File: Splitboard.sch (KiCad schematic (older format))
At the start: 5 parts

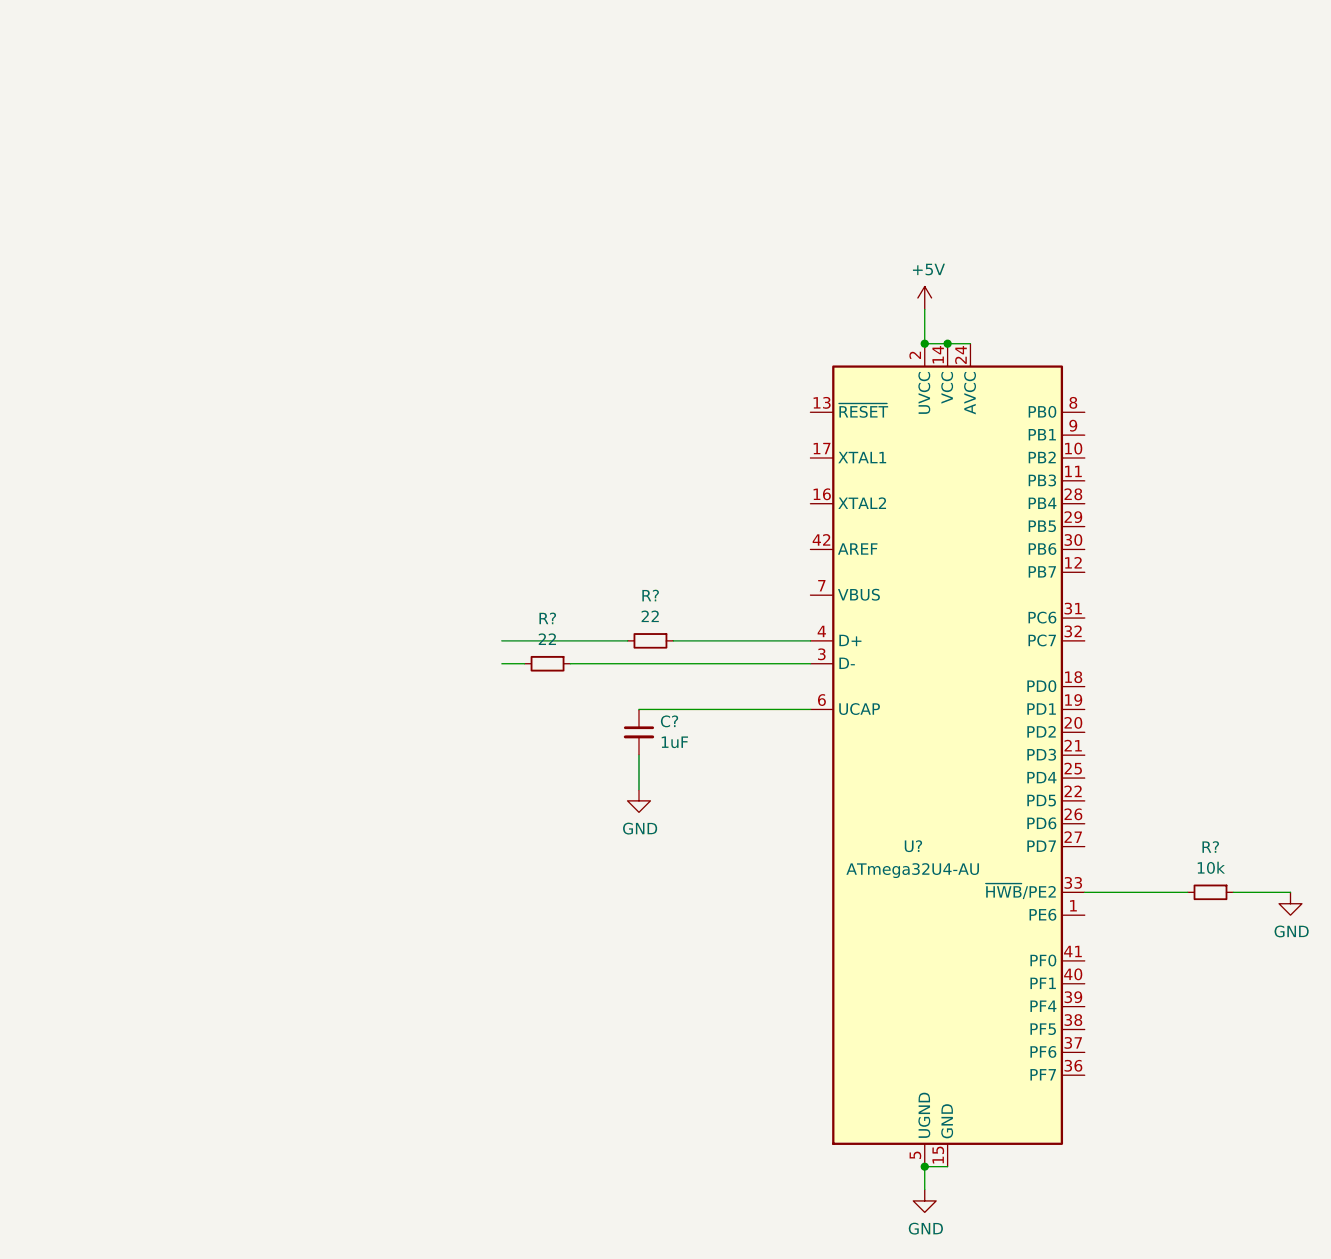
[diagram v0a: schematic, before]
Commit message: Add submodules
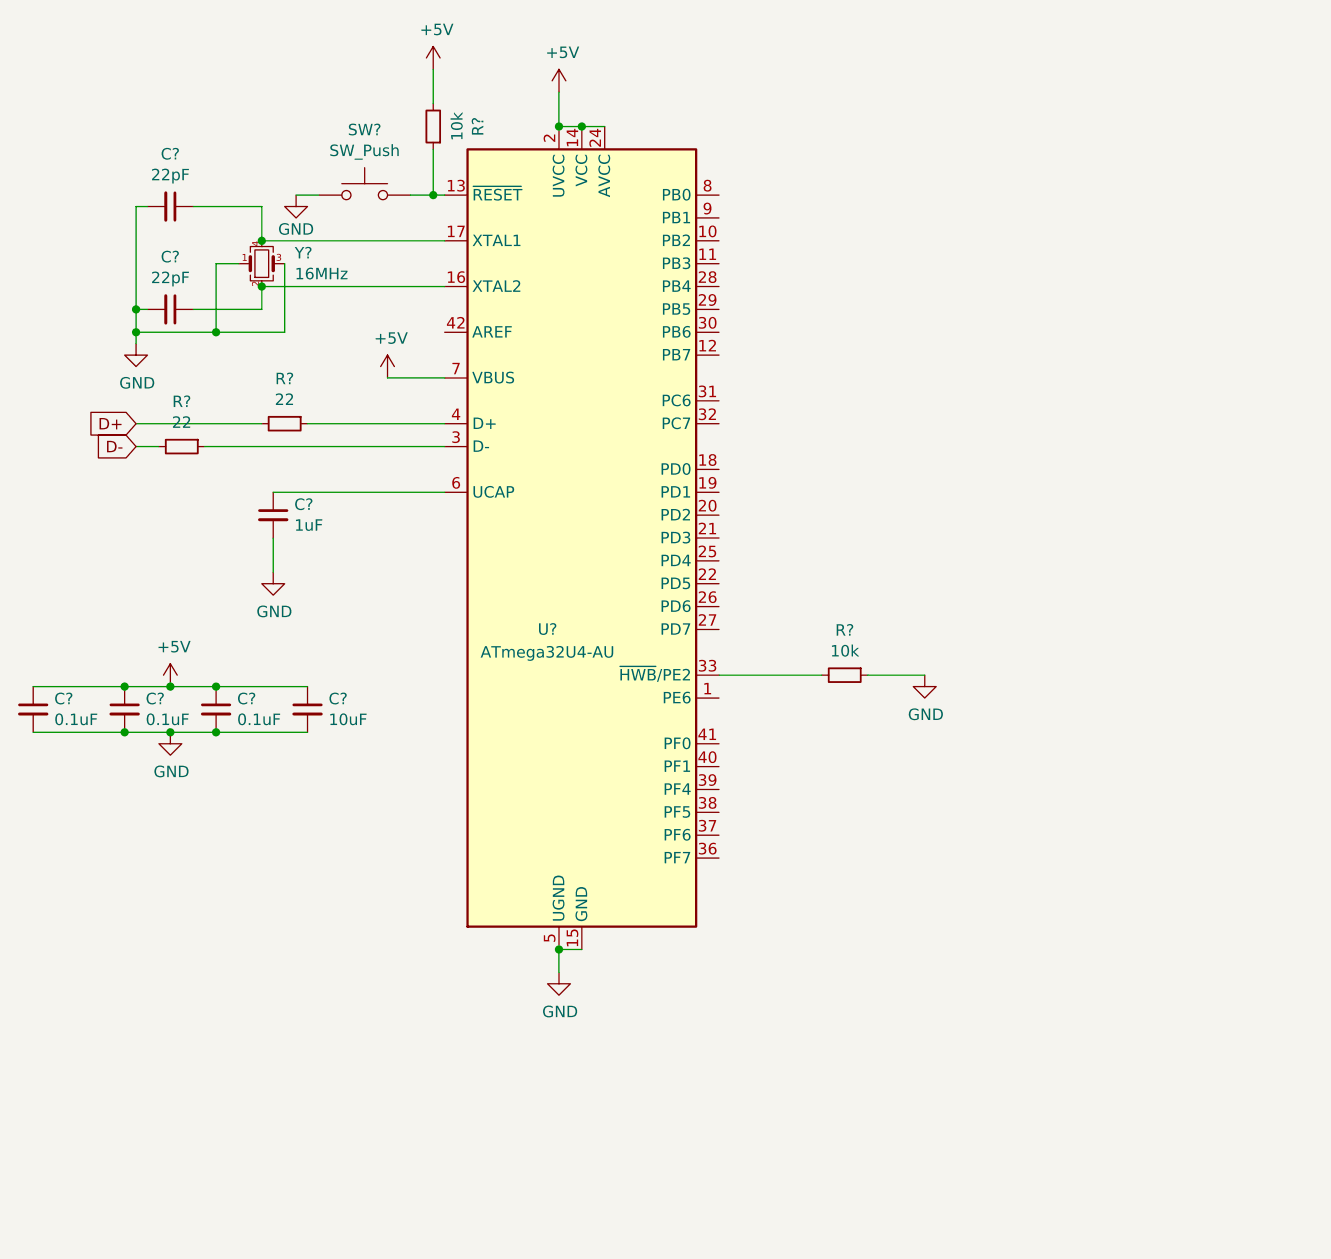
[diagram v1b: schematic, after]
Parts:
- added C? (x3): 0.1uF, symbol Device:C_Small
- added C?: 10uF, symbol Device:C_Small
- added C? (x2): 22pF, symbol Device:C_Small
- added R?: 10k, symbol Device:R_Small
- added SW?: SW_Push, symbol Switch:SW_Push
- added Y?: 16MHz, symbol Device:Crystal_GND24_Small
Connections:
- net labels added: D+, D-
- wire segments 13 -> 43
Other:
- moved on the sheet: C?, R?, U?

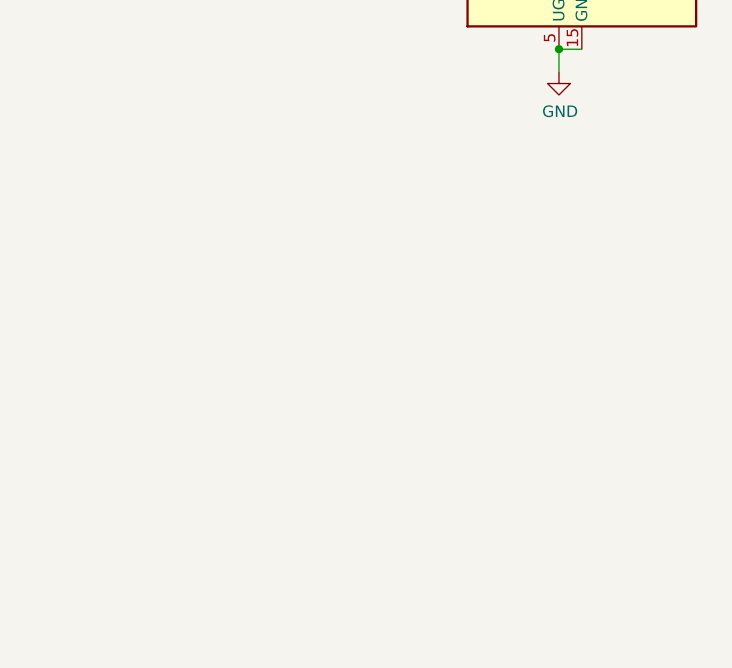
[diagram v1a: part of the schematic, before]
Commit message: basic layout no switches
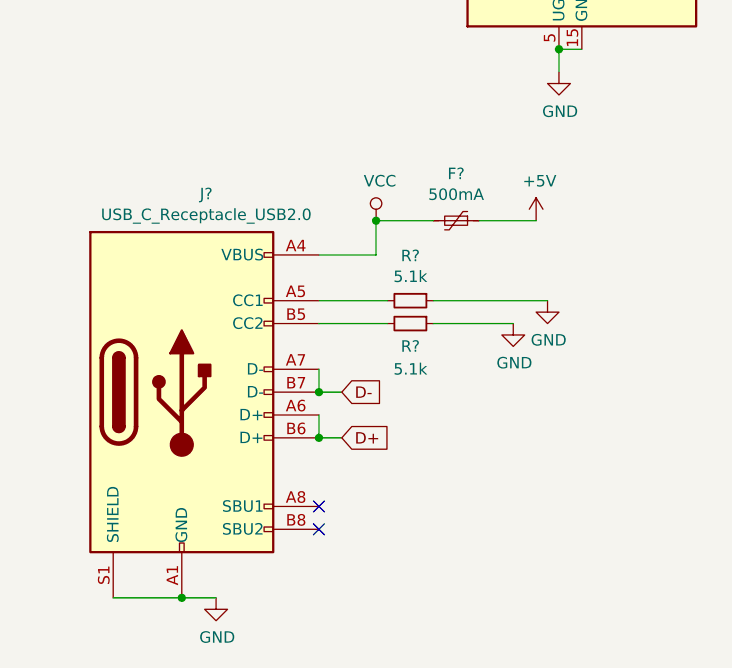
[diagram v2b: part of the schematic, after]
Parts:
- added F?: 500mA, symbol Device:Polyfuse_Small
- added J?: USB_C_Receptacle_USB2.0, symbol Connector:USB_C_Receptacle_USB2.0
- added R? (x2): 5.1k, symbol Device:R_Small
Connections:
- net +5V: now also F?.1
- net D+: now also J?.A6 (D+), J?.B6 (D+)
- net D-: now also J?.A7 (D-), J?.B7 (D-)
- net GND: now also J?.A1 (GND), J?.A12 (GND), J?.B1 (GND), J?.B12 (GND), J?.S1 (SHIELD), R?.1, R?.1
- new net: J?.A5 (CC1), R?.2
- new net: J?.B5 (CC2), R?.2
- new net VCC: F?.2, J?.A4 (VBUS), J?.A9 (VBUS), J?.B4 (VBUS), J?.B9 (VBUS)
- no-connect marks 0 -> 2
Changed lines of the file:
@@
 Text GLabel 1200 2400 0    50   Input ~ 0
 D-
+$Comp
+L Connector:USB_C_Receptacle_USB2.0 J?
+U 1 1 5F4D72AE
+P 1400 6100
+F 0 "J?" H 1507 6967 50  0000 C CNN
+F 1 "USB_C_Receptacle_USB2.0" H 1507 6876 50  0000 C CNN
+F 2 "" H 1550 6100 50  0001 C CNN
+F 3 "https://www.usb.org/sites/default/files/documents/usb_type-c.zip" H 1550 6100 50  0001 C CNN
+	1    1400 6100
+	1    0    0    -1
+$EndComp
+$Comp
+L Device:R_Small R?
+U 1 1 5F4DA8E6
+P 2400 5700
+F 0 "R?" V 2204 5700 50  0000 C CNN
+F 1 "5.1k" V 2295 5700 50  0000 C CNN
+F 2 "" H 2400 5700 50  0001 C CNN
+F 3 "~" H 2400 5700 50  0001 C CNN
+	1    2400 5700
+	0    1    1    0
+$EndComp
+$Comp
+L Device:R_Small R?
+U 1 1 5F4DB46A
+P 2400 5800
+F 0 "R?" V 2500 5800 50  0000 C CNN
+F 1 "5.1k" V 2600 5800 50  0000 C CNN
+F 2 "" H 2400 5800 50  0001 C CNN
+F 3 "~" H 2400 5800 50  0001 C CNN
+	1    2400 5800
+	0    1    1    0
+$EndComp
+$Comp
+L power:GND #PWR?
+U 1 1 5F4DBB17
+P 2850 5800
+F 0 "#PWR?" H 2850 5550 50  0001 C CNN
+F 1 "GND" H 2855 5627 50  0000 C CNN
+F 2 "" H 2850 5800 50  0001 C CNN
+F 3 "" H 2850 5800 50  0001 C CNN
+	1    2850 5800
+	1    0    0    -1
+$EndComp
+$Comp
+L power:GND #PWR?
+U 1 1 5F4DC6DD
+P 3000 5700
+F 0 "#PWR?" H 3000 5450 50  0001 C CNN
+F 1 "GND" H 3005 5527 50  0000 C CNN
+F 2 "" H 3000 5700 50  0001 C CNN
+F 3 "" H 3000 5700 50  0001 C CNN
+	1    3000 5700
+	1    0    0    -1
+$EndComp
+Wire Wire Line
+	3000 5700 2500 5700
+Wire Wire Line
+	2850 5800 2500 5800
+Wire Wire Line
+	2300 5800 2000 5800
+Wire Wire Line
+	2300 5700 2000 5700
+Wire Wire Line
+	2000 6000 2000 6100
+Wire Wire Line
+	2000 6100 2100 6100
+Connection ~ 2000 6100
+Wire Wire Line
+	2000 6200 2000 6300
+Wire Wire Line
+	2000 6300 2100 6300
+Connection ~ 2000 6300
+NoConn ~ 2000 6600
+NoConn ~ 2000 6700
+$Comp
+L power:VCC #PWR?
+U 1 1 5F4E5B6C
+P 2250 5350
+F 0 "#PWR?" H 2250 5200 50  0001 C CNN
+F 1 "VCC" H 2267 5523 50  0000 C CNN
+F 2 "" H 2250 5350 50  0001 C CNN
+F 3 "" H 2250 5350 50  0001 C CNN
+	1    2250 5350
+	1    0    0    -1
+$EndComp
+Wire Wire Line
+	2000 5500 2250 5500
+Wire Wire Line
+	2250 5500 2250 5350
+$Comp
+L Device:Polyfuse_Small F?
+U 1 1 5F4E76E9
+P 2600 5350
+F 0 "F?" V 2395 5350 50  0000 C CNN
+F 1 "500mA" V 2486 5350 50  0000 C CNN
+F 2 "" H 2650 5150 50  0001 L CNN
+F 3 "~" H 2600 5350 50  0001 C CNN
+	1    2600 5350
+	0    1    1    0
+$EndComp
+Wire Wire Line
+	2250 5350 2500 5350
+Connection ~ 2250 5350
+$Comp
+L power:+5V #PWR?
+U 1 1 5F4E9BB4
+P 2950 5350
+F 0 "#PWR?" H 2950 5200 50  0001 C CNN
+F 1 "+5V" H 2965 5523 50  0000 C CNN
+F 2 "" H 2950 5350 50  0001 C CNN
+F 3 "" H 2950 5350 50  0001 C CNN
+	1    2950 5350
+	1    0    0    -1
+$EndComp
+Wire Wire Line
+	2700 5350 2950 5350
+Text GLabel 2100 6300 2    50   Input ~ 0
+D+
+Text GLabel 2100 6100 2    50   Input ~ 0
+D-
+Wire Wire Line
+	1100 7000 1400 7000
+Connection ~ 1400 7000
+Wire Wire Line
+	1400 7000 1550 7000
+$Comp
+L power:GND #PWR?
+U 1 1 5F4EEDED
+P 1550 7000
+F 0 "#PWR?" H 1550 6750 50  0001 C CNN
+F 1 "GND" H 1555 6827 50  0000 C CNN
+F 2 "" H 1550 7000 50  0001 C CNN
+F 3 "" H 1550 7000 50  0001 C CNN
+	1    1550 7000
+	1    0    0    -1
+$EndComp
 $EndSCHEMATC

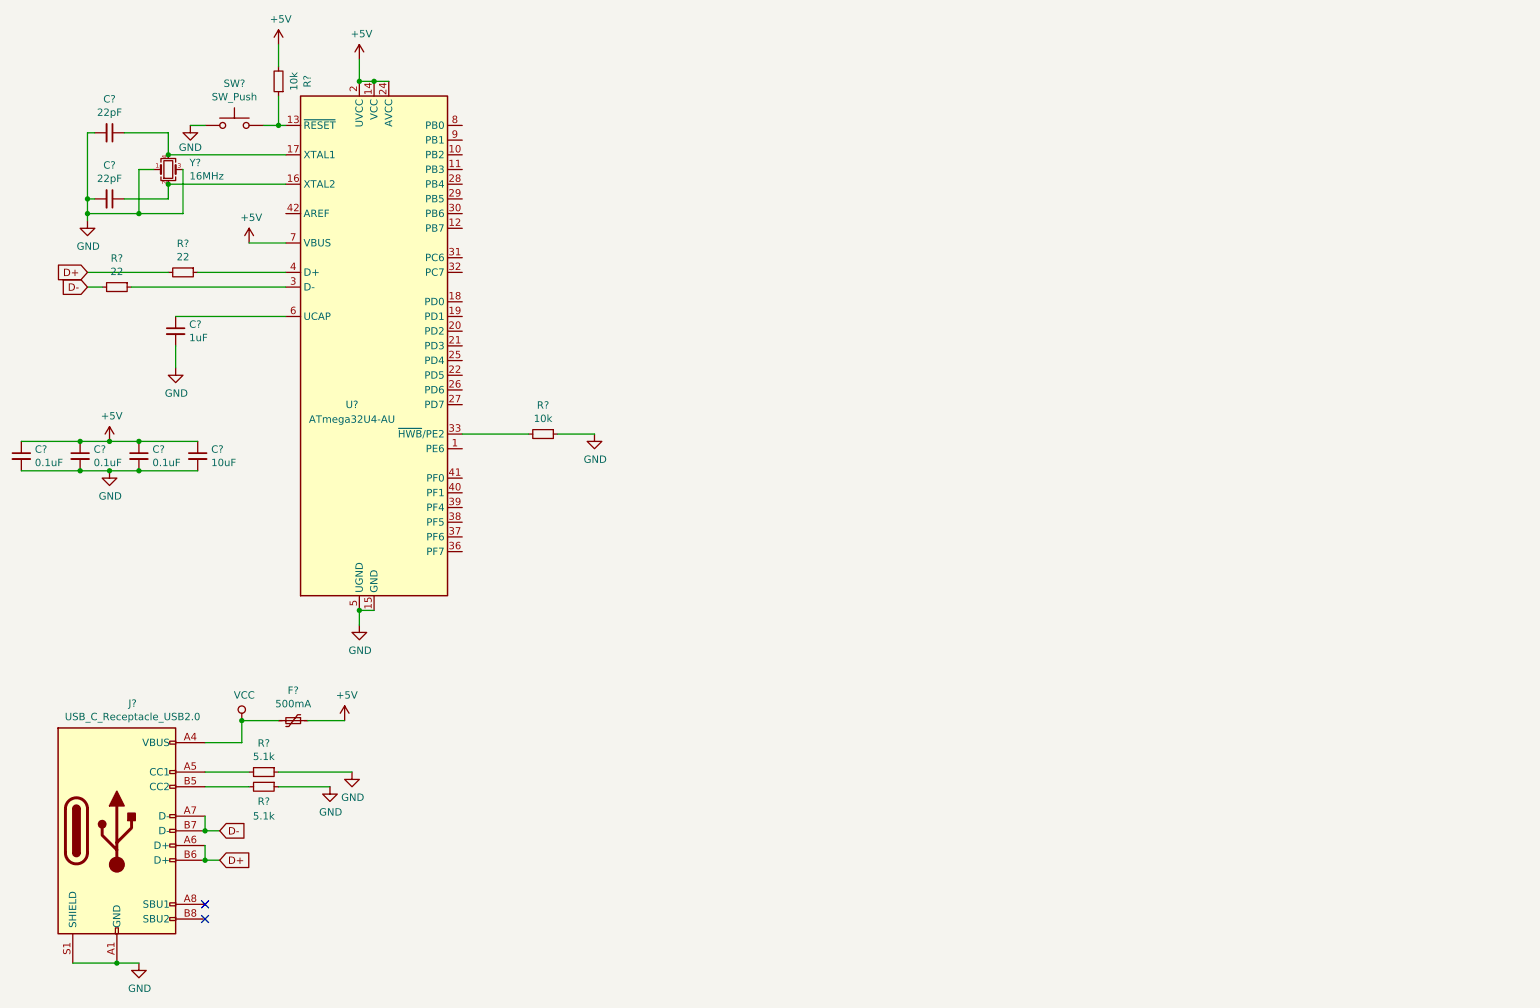
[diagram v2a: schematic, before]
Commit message: left side switch layout
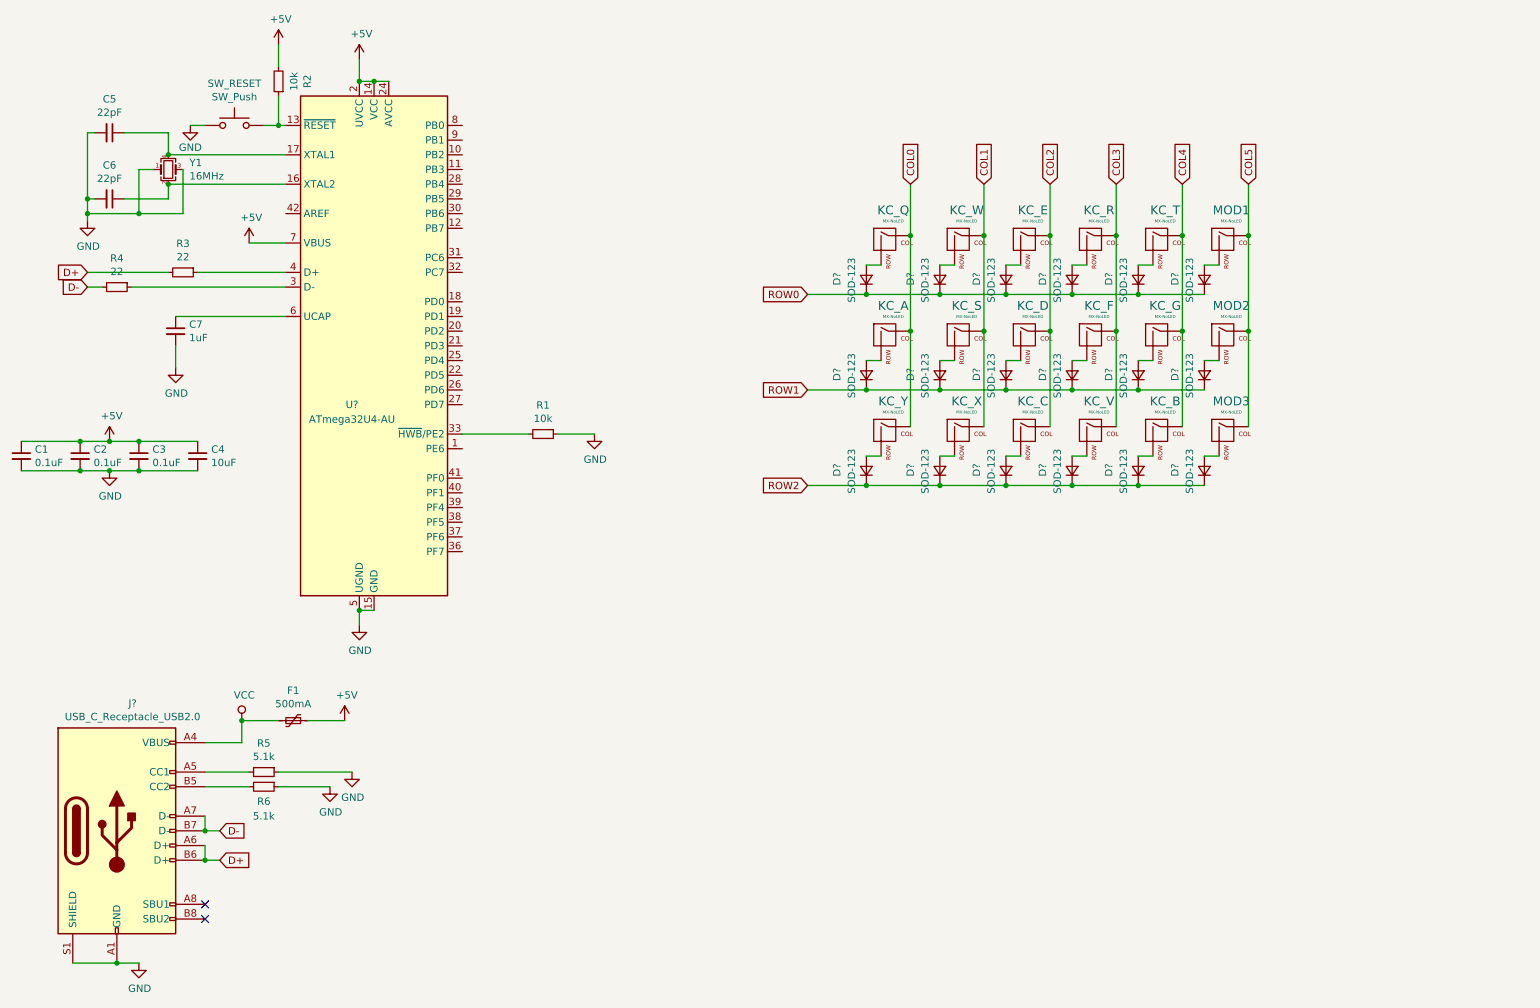
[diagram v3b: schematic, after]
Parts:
- added D? (x18): SOD-123, symbol Device:D_Small
- added KC_A, KC_B, KC_C, KC_D, KC_E, KC_F, KC_G, KC_Q, KC_R, KC_S, KC_T, KC_V, KC_W, KC_X, KC_Y, MOD1, MOD2, MOD3: MX-NoLED, symbol MX_Alps_Hybrid:MX-NoLED
- gave numbers to parts that had none: 16
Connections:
- new net: D?.2 (A), KC_Q.2 (ROW)
- new net: D?.2 (A), KC_W.2 (ROW)
- new net: D?.2 (A), KC_E.2 (ROW)
- new net: D?.2 (A), KC_R.2 (ROW)
- new net: D?.2 (A), KC_T.2 (ROW)
- new net: D?.2 (A), MOD1.2 (ROW)
- new net: D?.2 (A), KC_A.2 (ROW)
- new net: D?.2 (A), KC_S.2 (ROW)
- new net: D?.2 (A), KC_D.2 (ROW)
- new net: D?.2 (A), KC_F.2 (ROW)
- new net: D?.2 (A), KC_G.2 (ROW)
- new net: D?.2 (A), MOD2.2 (ROW)
- new net: D?.2 (A), KC_Y.2 (ROW)
- new net: D?.2 (A), KC_X.2 (ROW)
- new net: D?.2 (A), KC_C.2 (ROW)
- new net: D?.2 (A), KC_V.2 (ROW)
- new net: D?.2 (A), KC_B.2 (ROW)
- new net: D?.2 (A), MOD3.2 (ROW)
- new net COL0: KC_A.1 (COL), KC_Q.1 (COL), KC_Y.1 (COL)
- new net COL1: KC_S.1 (COL), KC_W.1 (COL), KC_X.1 (COL)
- new net COL2: KC_C.1 (COL), KC_D.1 (COL), KC_E.1 (COL)
- new net COL3: KC_F.1 (COL), KC_R.1 (COL), KC_V.1 (COL)
- new net COL4: KC_B.1 (COL), KC_G.1 (COL), KC_T.1 (COL)
- new net COL5: MOD1.1 (COL), MOD2.1 (COL), MOD3.1 (COL)
- new net ROW0: D?.1 (K), D?.1 (K), D?.1 (K), D?.1 (K), D?.1 (K), D?.1 (K)
- new net ROW1: D?.1 (K), D?.1 (K), D?.1 (K), D?.1 (K), D?.1 (K), D?.1 (K)
- new net ROW2: D?.1 (K), D?.1 (K), D?.1 (K), D?.1 (K), D?.1 (K), D?.1 (K)
